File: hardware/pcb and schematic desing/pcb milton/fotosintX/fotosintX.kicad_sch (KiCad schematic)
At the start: 12 parts, among them J4 TB_1X2, J5 TB_1X2, Q1 2N3904, U1 ESP32_DEVKITC, U2 L7805

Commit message: Mejorando pcb
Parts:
- added D1: 1N4007, Diode_THT:D_DO-41_SOD81_P10.16mm_Horizontal, symbol Diode:1N4007
- added H1, H2: Mounting_Hole, eestn5:hole_3mm, symbol eestn5:Mounting_Hole
- C1, C2: footprint eestn5:CAP_ELEC_8x11.5mm -> eestn5:CAP_0.1
- Q1: value 2N3904 -> PN2222A; footprint Package_TO_SOT_THT:TO-92_Inline -> Package_TO_SOT_THT:TO-92_Wide
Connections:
- net motor is gone; now on net +5V: J4.1, Q1.3 (C)
- net +5V: now also D1.1 (K), D1.2 (A)
- net SCL: now also LCDOLED1.1 (Pin_1); no longer LCDOLED1.2 (Pin_2)
- net SDA: now also LCDOLED1.2 (Pin_2); no longer LCDOLED1.1 (Pin_1)
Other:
- moved on the sheet: R1
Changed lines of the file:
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@@
   (junction (at 224.79 71.12) (diameter 0) (color 0 0 0 0)
   )
+  (junction (at 177.8 78.74) (diameter 0) (color 0 0 0 0)
+  )
+  (junction (at 177.8 66.04) (diameter 0) (color 0 0 0 0)
+  )
   (junction (at 247.65 71.12) (diameter 0) (color 0 0 0 0)
   )
@@
     (stroke (width 0) (type default))
   )
+  (wire (pts (xy 172.72 66.04) (xy 172.72 68.58))
+    (stroke (width 0) (type default))
+  )
   (wire (pts (xy 224.79 71.12) (xy 224.79 73.66))
     (stroke (width 0) (type default))
   )
+  (wire (pts (xy 177.8 63.5) (xy 177.8 66.04))
+    (stroke (width 0) (type default))
+  )
   (wire (pts (xy 247.65 71.12) (xy 247.65 73.66))
     (stroke (width 0) (type default))
@@
     (stroke (width 0) (type default))
   )
-  (wire (pts (xy 157.48 85.09) (xy 160.02 85.09))
+  (wire (pts (xy 160.02 85.09) (xy 162.56 85.09))
     (stroke (width 0) (type default))
   )
@@
     (stroke (width 0) (type default))
   )
-  (wire (pts (xy 181.61 57.15) (xy 181.61 54.61))
+  (wire (pts (xy 181.61 52.07) (xy 181.61 57.15))
     (stroke (width 0) (type default))
   )
@@
     (stroke (width 0) (type default))
   )
+  (wire (pts (xy 177.8 66.04) (xy 177.8 78.74))
+    (stroke (width 0) (type default))
+  )
   (wire (pts (xy 140.97 111.76) (xy 140.97 109.22))
     (stroke (width 0) (type default))
@@
     (stroke (width 0) (type default))
   )
+  (wire (pts (xy 177.8 78.74) (xy 177.8 80.01))
+    (stroke (width 0) (type default))
+  )
+  (wire (pts (xy 172.72 76.2) (xy 172.72 78.74))
+    (stroke (width 0) (type default))
+  )
   (wire (pts (xy 144.78 68.58) (xy 138.43 68.58))
     (stroke (width 0) (type default))
@@
     (stroke (width 0) (type default))
   )
-  (wire (pts (xy 167.64 85.09) (xy 170.18 85.09))
-    (stroke (width 0) (type default))
-  )
   (wire (pts (xy 146.05 109.22) (xy 146.05 113.03))
     (stroke (width 0) (type default))
   )
+  (wire (pts (xy 177.8 78.74) (xy 172.72 78.74))
+    (stroke (width 0) (type default))
+  )
   (wire (pts (xy 247.65 81.28) (xy 247.65 83.82))
     (stroke (width 0) (type default))
@@
     (stroke (width 0) (type default))
   )
+  (wire (pts (xy 172.72 66.04) (xy 177.8 66.04))
+    (stroke (width 0) (type default))
+  )
   (wire (pts (xy 171.45 53.34) (xy 171.45 58.42))
     (stroke (width 0) (type default))
   )
-  (label "ON" (at 157.48 85.09 180) (fields_autoplaced)
+  (label "ON" (at 160.02 85.09 180) (fields_autoplaced)
     (effects (font (size 1.27 1.27)) (justify right bottom))
   )
@@
     (effects (font (size 1.27 1.27)) (justify right bottom))
   )
-  (label "SCL" (at 124.46 90.17 270) (fields_autoplaced)
+  (label "SCL" (at 121.92 90.17 270) (fields_autoplaced)
     (effects (font (size 1.27 1.27)) (justify right bottom))
   )
@@
     (effects (font (size 1.27 1.27)) (justify right bottom))
   )
-  (label "motor" (at 181.61 54.61 0) (fields_autoplaced)
+  (label "motor" (at 181.61 57.15 0) (fields_autoplaced)
     (effects (font (size 1.27 1.27)) (justify left bottom))
   )
@@
     (effects (font (size 1.27 1.27)) (justify left bottom))
   )
-  (label "SDA" (at 121.92 90.17 270) (fields_autoplaced)
+  (label "SDA" (at 124.46 90.17 270) (fields_autoplaced)
     (effects (font (size 1.27 1.27)) (justify right bottom))
   )
@@
     (effects (font (size 1.27 1.27)) (justify left bottom))
   )
-  (label "motor" (at 177.8 80.01 0) (fields_autoplaced)
+  (label "motor" (at 177.8 63.5 0) (fields_autoplaced)
     (effects (font (size 1.27 1.27)) (justify left bottom))
   )
@@
       (effects (font (size 1.27 1.27)) (justify left))
     )
-    (property "Footprint" "eestn5:CAP_ELEC_8x11.5mm" (at 225.7552 81.28 0)
+    (property "Footprint" "eestn5:CAP_0.1" (at 225.7552 81.28 0)
       (effects (font (size 1.27 1.27)) hide)
     )
@@
     )
   )
+  (symbol (lib_id "eestn5:Mounting_Hole") (at 193.04 102.87 0) (unit 1)
+    (in_bom yes) (on_board yes) (dnp no) (fields_autoplaced)
+    (property "Reference" "H1" (at 195.58 103.505 0)
+      (effects (font (size 1.27 1.27)) (justify left))
+    )
+    (property "Value" "Mounting_Hole" (at 193.04 99.695 0)
+      (effects (font (size 1.27 1.27)) hide)
+    )
+    (property "Footprint" "eestn5:hole_3mm" (at 193.04 102.87 0)
+      (effects (font (size 1.524 1.524)) hide)
+    )
+    (property "Datasheet" "" (at 193.04 102.87 0)
+      (effects (font (size 1.524 1.524)) hide)
+    )
+    (instances
+      (project "fotosintX"
+        (path "/95f6a210-5d10-43c2-9842-1e5a2410688b"
+          (reference "H1") (unit 1)
+        )
+      )
+    )
+  )
   (symbol (lib_id "Device:C") (at 247.65 77.47 0) (unit 1)
     (in_bom yes) (on_board yes) (dnp no) (fields_autoplaced)
@@
       (effects (font (size 1.27 1.27)) (justify left))
     )
-    (property "Footprint" "eestn5:CAP_ELEC_8x11.5mm" (at 248.6152 81.28 0)
+    (property "Footprint" "eestn5:CAP_0.1" (at 248.6152 81.28 0)
       (effects (font (size 1.27 1.27)) hide)
     )
@@
       (effects (font (size 1.27 1.27)) (justify left))
     )
-    (property "Value" "2N3904" (at 180.34 86.995 0)
-      (effects (font (size 1.27 1.27)) (justify left))
-    )
-    (property "Footprint" "Package_TO_SOT_THT:TO-92_Inline" (at 180.34 86.995 0)
+    (property "Value" "PN2222A" (at 180.34 86.995 0)
+      (effects (font (size 1.27 1.27)) (justify left))
+    )
+    (property "Footprint" "Package_TO_SOT_THT:TO-92_Wide" (at 180.34 86.995 0)
       (effects (font (size 1.27 1.27) italic) (justify left) hide)
     )
@@
     )
   )
-  (symbol (lib_id "Device:R") (at 163.83 85.09 270) (unit 1)
-    (in_bom yes) (on_board yes) (dnp no) (fields_autoplaced)
-    (property "Reference" "R1" (at 163.83 80.01 90)
-      (effects (font (size 1.27 1.27)))
-    )
-    (property "Value" "R" (at 163.83 82.55 90)
-      (effects (font (size 1.27 1.27)))
-    )
-    (property "Footprint" "eestn5:RES0.3" (at 163.83 83.312 90)
-      (effects (font (size 1.27 1.27)) hide)
-    )
-    (property "Datasheet" "~" (at 163.83 85.09 0)
+  (symbol (lib_id "Device:R") (at 166.37 85.09 270) (unit 1)
+    (in_bom yes) (on_board yes) (dnp no) (fields_autoplaced)
+    (property "Reference" "R1" (at 166.37 80.01 90)
+      (effects (font (size 1.27 1.27)))
+    )
+    (property "Value" "R" (at 166.37 82.55 90)
+      (effects (font (size 1.27 1.27)))
+    )
+    (property "Footprint" "eestn5:RES0.3" (at 166.37 83.312 90)
+      (effects (font (size 1.27 1.27)) hide)
+    )
+    (property "Datasheet" "~" (at 166.37 85.09 0)
       (effects (font (size 1.27 1.27)) hide)
     )
@@
     )
   )
+  (symbol (lib_id "eestn5:Mounting_Hole") (at 201.93 102.87 0) (unit 1)
+    (in_bom yes) (on_board yes) (dnp no) (fields_autoplaced)
+    (property "Reference" "H2" (at 204.47 103.505 0)
+      (effects (font (size 1.27 1.27)) (justify left))
+    )
+    (property "Value" "Mounting_Hole" (at 201.93 99.695 0)
+      (effects (font (size 1.27 1.27)) hide)
+    )
+    (property "Footprint" "eestn5:hole_3mm" (at 201.93 102.87 0)
+      (effects (font (size 1.524 1.524)) hide)
+    )
+    (property "Datasheet" "" (at 201.93 102.87 0)
+      (effects (font (size 1.524 1.524)) hide)
+    )
+    (instances
+      (project "fotosintX"
+        (path "/95f6a210-5d10-43c2-9842-1e5a2410688b"
+          (reference "H2") (unit 1)
+        )
+      )
+    )
+  )
   (symbol (lib_id "power:Earth") (at 213.36 62.23 0) (unit 1)
     (in_bom yes) (on_board yes) (dnp no) (fields_autoplaced)
@@
     )
   )
+  (symbol (lib_id "Diode:1N4007") (at 172.72 72.39 270) (unit 1)
+    (in_bom yes) (on_board yes) (dnp no)
+    (property "Reference" "D1" (at 166.37 72.39 90)
+      (effects (font (size 1.27 1.27)) (justify left))
+    )
+    (property "Value" "1N4007" (at 163.83 74.93 90)
+      (effects (font (size 1.27 1.27)) (justify left))
+    )
+    (property "Footprint" "Diode_THT:D_DO-41_SOD81_P10.16mm_Horizontal" (at 168.275 72.39 0)
+      (effects (font (size 1.27 1.27)) hide)
+    )
+    (property "Datasheet" "http://www.vishay.com/docs/88503/1n4001.pdf" (at 172.72 72.39 0)
+      (effects (font (size 1.27 1.27)) hide)
+    )
+    (property "Sim.Device" "D" (at 172.72 72.39 0)
+      (effects (font (size 1.27 1.27)) hide)
+    )
+    (property "Sim.Pins" "1=K 2=A" (at 172.72 72.39 0)
+      (effects (font (size 1.27 1.27)) hide)
+    )
+    (pin "1")
+    (pin "2")
+    (instances
+      (project "fotosintX"
+        (path "/95f6a210-5d10-43c2-9842-1e5a2410688b"
+          (reference "D1") (unit 1)
+        )
+      )
+    )
+  )
   (symbol (lib_id "eestn5:Conn_01X03") (at 121.92 59.69 90) (unit 1)
     (in_bom yes) (on_board yes) (dnp no)
@@
         )
       )
+    )
+  )
+  (symbol (lib_id "power:+5V") (at 181.61 52.07 0) (unit 1)
+    (in_bom yes) (on_board yes) (dnp no)
+    (property "Reference" "#PWR021" (at 181.61 55.88 0)
+      (effects (font (size 1.27 1.27)) hide)
+    )
+    (property "Value" "+5V" (at 184.15 52.07 0)
+      (effects (font (size 1.27 1.27)))
+    )
+    (property "Footprint" "" (at 181.61 52.07 0)
+      (effects (font (size 1.27 1.27)) hide)
+    )
+    (property "Datasheet" "" (at 181.61 52.07 0)
+      (effects (font (size 1.27 1.27)) hide)
+    )
+    (pin "1")
+    (instances
+      (project "fotosintX"
+        (path "/95f6a210-5d10-43c2-9842-1e5a2410688b"
+          (reference "#PWR021") (unit 1)
+        )
+      )

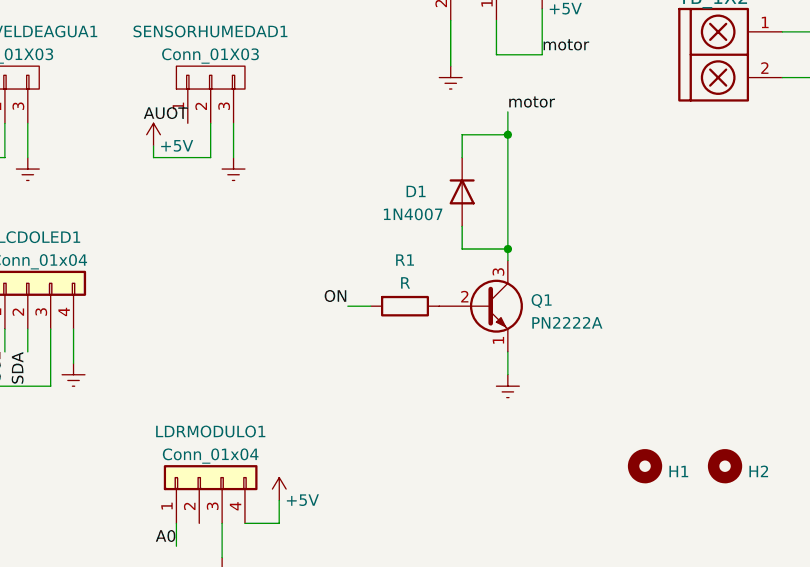
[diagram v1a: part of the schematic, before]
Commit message: me olvide de ponerle el valor ala resistencia :V
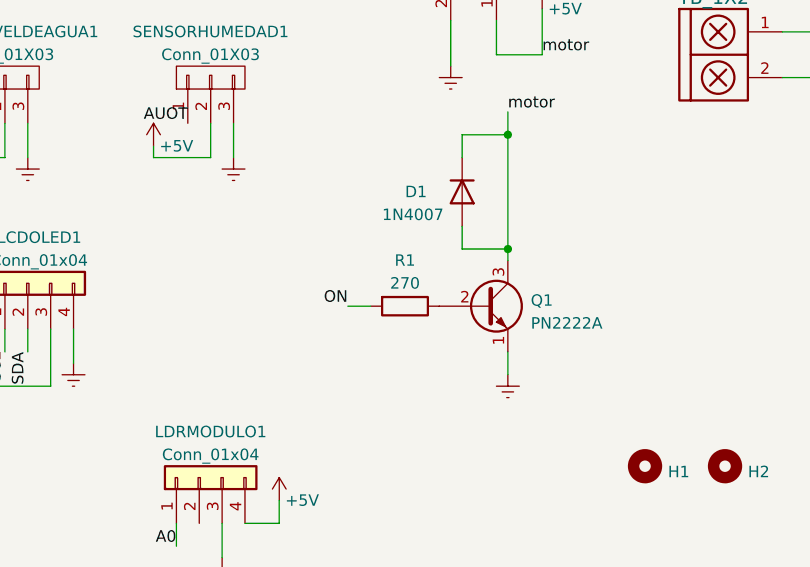
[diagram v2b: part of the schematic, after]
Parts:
- R1: value R -> 270
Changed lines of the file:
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@@
       (effects (font (size 1.27 1.27)))
     )
-    (property "Value" "R" (at 166.37 82.55 90)
+    (property "Value" "270" (at 166.37 82.55 90)
       (effects (font (size 1.27 1.27)))
     )

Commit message: arregle el schematic
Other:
- note added: "BORNERAS DE SALIDA"
- note added: "CIRCUITO PARA CAMBIAR LA TIERRA DEL MOTOR"
- note added: "MICROCONTROLADOR"
- note added: "PINERAS PERTENECIENTES A MODULOS"
- note added: "REGULADOR DE TENSION"
- moved on the sheet: C1, C2, D1, H1, H2, J4, J5, LCDOLED1, LDRMODULO1, Q1, R1, SENSORHUMEDAD1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

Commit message: pcb modified
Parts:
- added J1: Conn_01x02_Pin, Connector_PinHeader_2.54mm:PinHeader_1x02_P2.54mm_Vertical, symbol Connector:Conn_01x02_Pin
- added M1: Motor_DC, symbol Motor:Motor_DC
- R1: value 270 -> 1500
- renumbered SENSORNIVELDEAGUA1 to CAUDALIMETRO1
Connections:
- net +5V: now also J1.1 (Pin_1), M1.1 (+); no longer D1.2 (A), Q1.3 (C)
- new net motor-: D1.2 (A), J1.2 (Pin_2), M1.2 (-), Q1.3 (C)
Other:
- moved on the sheet: D1, J4, J5

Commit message: edit pcb print pdf
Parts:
- C1, C2: footprint eestn5:CAP_0.1 -> EESTN5:CAP_0.1
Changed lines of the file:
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@@
       (effects (font (size 1.27 1.27)) (justify left))
     )
-    (property "Footprint" "eestn5:CAP_0.1" (at 171.1452 39.37 0)
+    (property "Footprint" "EESTN5:CAP_0.1" (at 171.1452 39.37 0)
       (effects (font (size 1.27 1.27)) hide)
     )
@@
       (effects (font (size 1.27 1.27)) (justify left))
     )
-    (property "Footprint" "eestn5:CAP_0.1" (at 194.0052 39.37 0)
+    (property "Footprint" "EESTN5:CAP_0.1" (at 194.0052 39.37 0)
       (effects (font (size 1.27 1.27)) hide)
     )

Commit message: PCB terminado
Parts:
- removed J5: TB_1X2, eestn5:BORNERA2, symbol eestn5:TB_1X2
- added J2: Jack-DC, jack dc 12v 2 patas:CUI_PJ-037AH, symbol Connector:Jack-DC
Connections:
- net +12V: now also J2.1
- net +5V: no longer LDRMODULO1.4 (Pin_4)
- net Earth: now also J2.2
- net SCL: now also LCDOLED1.2 (Pin_2); no longer LCDOLED1.1 (Pin_1)
- net SDA: now also LCDOLED1.1 (Pin_1); no longer LCDOLED1.2 (Pin_2)
- net SERIAL: now also U1.5 (IO34); no longer U1.6 (IO35)
- net +3.3V: now reaches U1.1 (3V3)
- net +3.3V: now also LDRMODULO1.4 (Pin_4)
- net AUOT renamed V-OUT
- net V-OUT: now also U1.6 (IO35); no longer U1.5 (IO34)
